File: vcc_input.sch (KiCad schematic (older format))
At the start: 2 parts

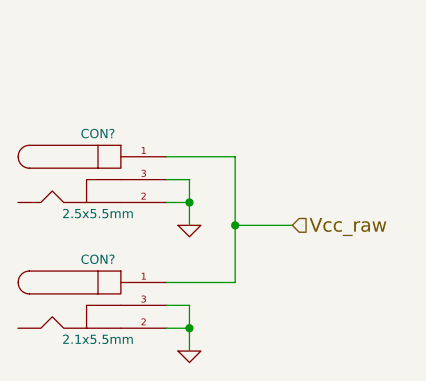
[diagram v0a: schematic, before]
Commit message: breaking Vee out into sub sheets
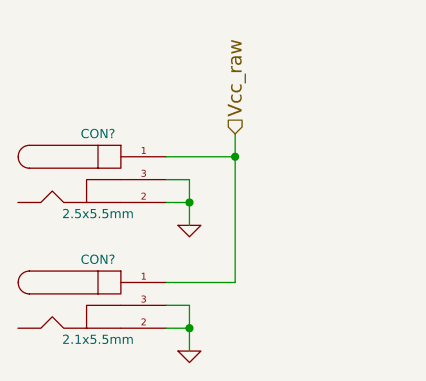
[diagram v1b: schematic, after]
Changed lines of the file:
@@
 $Descr A4 11693 8268
 encoding utf-8
-Sheet 2 4
+Sheet 2 7
 Title ""
 Date "29 mar 2014"
@@
 	1    0    0    -1
 $EndComp
-Text HLabel 6200 3850 2    60   Input ~ 0
+Text HLabel 5950 3450 1    60   Input ~ 0
 Vcc_raw
 Wire Wire Line
-	5950 3550 5950 4100
-Wire Wire Line
-	6200 3850 5950 3850
-Connection ~ 5950 3850
+	5950 3450 5950 4100
+Connection ~ 5950 3550
 $EndSCHEMATC
